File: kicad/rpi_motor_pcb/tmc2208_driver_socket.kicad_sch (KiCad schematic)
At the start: 6 parts

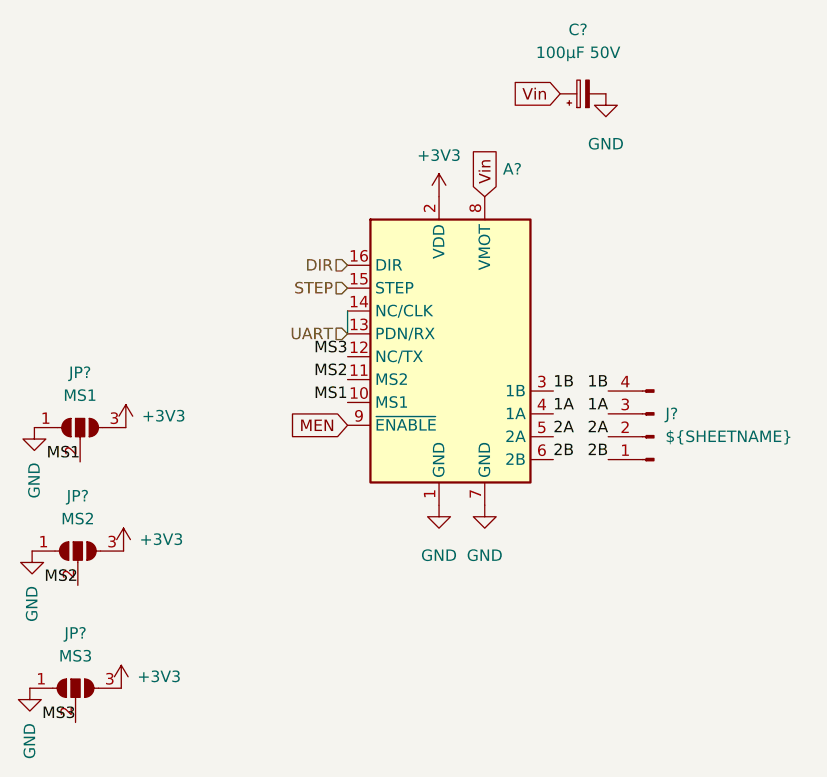
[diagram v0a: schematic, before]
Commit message: rpi_motor_pcb: 6 axis version
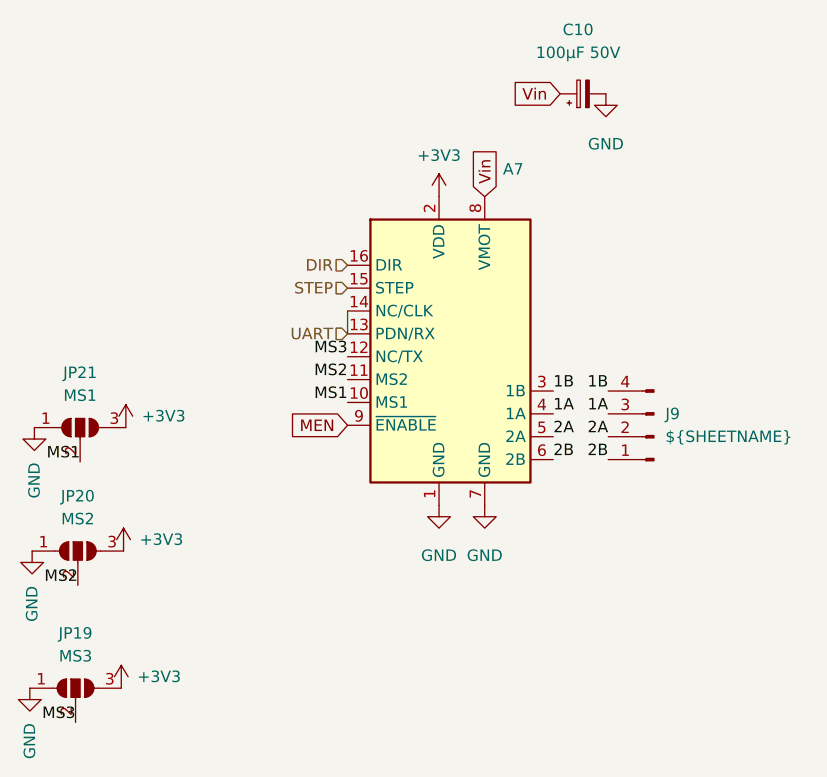
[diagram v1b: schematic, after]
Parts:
- gave numbers to parts that had none: 6
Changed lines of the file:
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@@
   (symbol (lib_id "power:+3V3") (at 59.944 75.692 0) (unit 1)
     (in_bom yes) (on_board yes) (fields_autoplaced)
-    (property "Reference" "#PWR?" (id 0) (at 59.944 79.502 0)
+    (property "Reference" "#PWR071" (id 0) (at 59.944 79.502 0)
       (effects (font (size 1.27 1.27)) hide)
     )
@@
   (symbol (lib_id "power:GND") (at 49.276 104.648 0) (unit 1)
     (in_bom yes) (on_board yes)
-    (property "Reference" "#PWR?" (id 0) (at 49.276 110.998 0)
+    (property "Reference" "#PWR04" (id 0) (at 49.276 110.998 0)
       (effects (font (size 1.27 1.27)) hide)
     )
@@
   (symbol (lib_id "Jumper:SolderJumper_3_Open") (at 54.356 104.648 0) (unit 1)
     (in_bom yes) (on_board yes) (fields_autoplaced)
-    (property "Reference" "JP?" (id 0) (at 54.356 98.552 0))
+    (property "Reference" "JP19" (id 0) (at 54.356 98.552 0))
     (property "Value" "MS3" (id 1) (at 54.356 101.092 0))
     (property "Footprint" "Jumper:SolderJumper-3_P1.3mm_Open_RoundedPad1.0x1.5mm" (id 2) (at 54.356 104.648 0)
@@
   (symbol (lib_id "power:+3V3") (at 59.436 104.648 0) (unit 1)
     (in_bom yes) (on_board yes) (fields_autoplaced)
-    (property "Reference" "#PWR?" (id 0) (at 59.436 108.458 0)
+    (property "Reference" "#PWR021" (id 0) (at 59.436 108.458 0)
       (effects (font (size 1.27 1.27)) hide)
     )
@@
   (symbol (lib_id "power:+3V3") (at 94.742 50.038 0) (unit 1)
     (in_bom yes) (on_board yes) (fields_autoplaced)
-    (property "Reference" "#PWR?" (id 0) (at 94.742 53.848 0)
+    (property "Reference" "#PWR080" (id 0) (at 94.742 53.848 0)
       (effects (font (size 1.27 1.27)) hide)
     )
@@
   (symbol (lib_id "power:GND") (at 113.284 38.608 0) (unit 1)
     (in_bom yes) (on_board yes) (fields_autoplaced)
-    (property "Reference" "#PWR?" (id 0) (at 113.284 44.958 0)
+    (property "Reference" "#PWR093" (id 0) (at 113.284 44.958 0)
       (effects (font (size 1.27 1.27)) hide)
     )
@@
   (symbol (lib_id "TMCSockets:MKS_TMC2208") (at 96.012 66.548 0) (unit 1)
     (in_bom yes) (on_board yes) (fields_autoplaced)
-    (property "Reference" "A?" (id 0) (at 101.8414 46.99 0)
+    (property "Reference" "A7" (id 0) (at 101.8414 46.99 0)
       (effects (font (size 1.27 1.27)) (justify left))
     )
@@
   (symbol (lib_id "power:GND") (at 99.822 84.328 0) (unit 1)
     (in_bom yes) (on_board yes) (fields_autoplaced)
-    (property "Reference" "#PWR?" (id 0) (at 99.822 90.678 0)
+    (property "Reference" "#PWR082" (id 0) (at 99.822 90.678 0)
       (effects (font (size 1.27 1.27)) hide)
     )
@@
   (symbol (lib_id "Jumper:SolderJumper_3_Open") (at 54.864 75.692 0) (unit 1)
     (in_bom yes) (on_board yes)
-    (property "Reference" "JP?" (id 0) (at 54.864 69.596 0))
+    (property "Reference" "JP21" (id 0) (at 54.864 69.596 0))
     (property "Value" "MS1" (id 1) (at 54.864 72.136 0))
     (property "Footprint" "Jumper:SolderJumper-3_P1.3mm_Open_RoundedPad1.0x1.5mm" (id 2) (at 54.864 75.692 0)
@@
   (symbol (lib_id "power:+3V3") (at 59.69 89.408 0) (unit 1)
     (in_bom yes) (on_board yes) (fields_autoplaced)
-    (property "Reference" "#PWR?" (id 0) (at 59.69 93.218 0)
+    (property "Reference" "#PWR026" (id 0) (at 59.69 93.218 0)
       (effects (font (size 1.27 1.27)) hide)
     )
@@
   (symbol (lib_id "power:GND") (at 94.742 84.328 0) (unit 1)
     (in_bom yes) (on_board yes) (fields_autoplaced)
-    (property "Reference" "#PWR?" (id 0) (at 94.742 90.678 0)
+    (property "Reference" "#PWR081" (id 0) (at 94.742 90.678 0)
       (effects (font (size 1.27 1.27)) hide)
     )
@@
   (symbol (lib_id "Connector:Conn_01x04_Male") (at 118.618 76.708 180) (unit 1)
     (in_bom yes) (on_board yes) (fields_autoplaced)
-    (property "Reference" "J?" (id 0) (at 119.888 74.1679 0)
+    (property "Reference" "J9" (id 0) (at 119.888 74.1679 0)
       (effects (font (size 1.27 1.27)) (justify right))
     )
@@
   (symbol (lib_id "power:GND") (at 49.784 75.692 0) (unit 1)
     (in_bom yes) (on_board yes)
-    (property "Reference" "#PWR?" (id 0) (at 49.784 82.042 0)
+    (property "Reference" "#PWR016" (id 0) (at 49.784 82.042 0)
       (effects (font (size 1.27 1.27)) hide)
     )
@@
   (symbol (lib_id "Jumper:SolderJumper_3_Open") (at 54.61 89.408 0) (unit 1)
     (in_bom yes) (on_board yes) (fields_autoplaced)
-    (property "Reference" "JP?" (id 0) (at 54.61 83.312 0))
+    (property "Reference" "JP20" (id 0) (at 54.61 83.312 0))
     (property "Value" "MS2" (id 1) (at 54.61 85.852 0))
     (property "Footprint" "Jumper:SolderJumper-3_P1.3mm_Open_RoundedPad1.0x1.5mm" (id 2) (at 54.61 89.408 0)
@@
   (symbol (lib_id "power:GND") (at 49.53 89.408 0) (unit 1)
     (in_bom yes) (on_board yes)
-    (property "Reference" "#PWR?" (id 0) (at 49.53 95.758 0)
+    (property "Reference" "#PWR011" (id 0) (at 49.53 95.758 0)
       (effects (font (size 1.27 1.27)) hide)
     )
@@
   (symbol (lib_id "Device:C_Polarized_Small") (at 110.744 38.608 90) (unit 1)
     (in_bom yes) (on_board yes) (fields_autoplaced)
-    (property "Reference" "C?" (id 0) (at 110.1979 31.496 90))
+    (property "Reference" "C10" (id 0) (at 110.1979 31.496 90))
     (property "Value" "100µF 50V" (id 1) (at 110.1979 34.036 90))
     (property "Footprint" "Capacitor_SMD:CP_Elec_6.3x7.7" (id 2) (at 110.744 38.608 0)
